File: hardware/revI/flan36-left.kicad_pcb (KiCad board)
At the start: 2 copper layers, 113.4 x 91.3 mm, 46 parts, among them J1 BATTERY_PIGTAIL, J2 nice!view, K01 KEYSW, K02 KEYSW, K03 KEYSW, K04 KEYSW, K05 KEYSW, K11 KEYSW, K12 KEYSW, K13 KEYSW, K14 KEYSW, K15 KEYSW, K21 KEYSW, K22 KEYSW, K23 KEYSW, K24 KEYSW, K25 KEYSW, K30 KEYSW, K31 KEYSW, K32 KEYSW, SW1 SW_SPDT_PCM12, SW2 SW_SPST_TL3342, U1 nice!nano v2

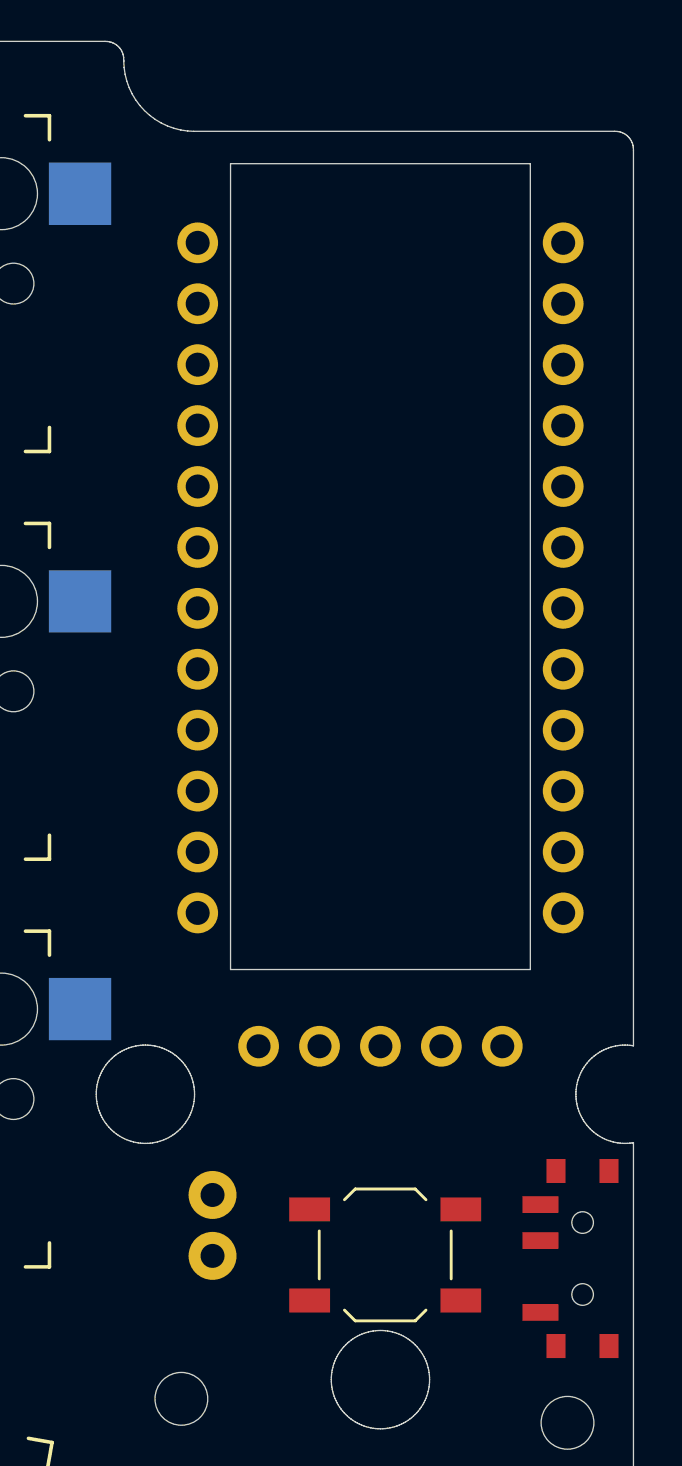
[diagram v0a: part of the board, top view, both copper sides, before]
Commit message: Lower electronics stack and add flush multicolor frame inlays
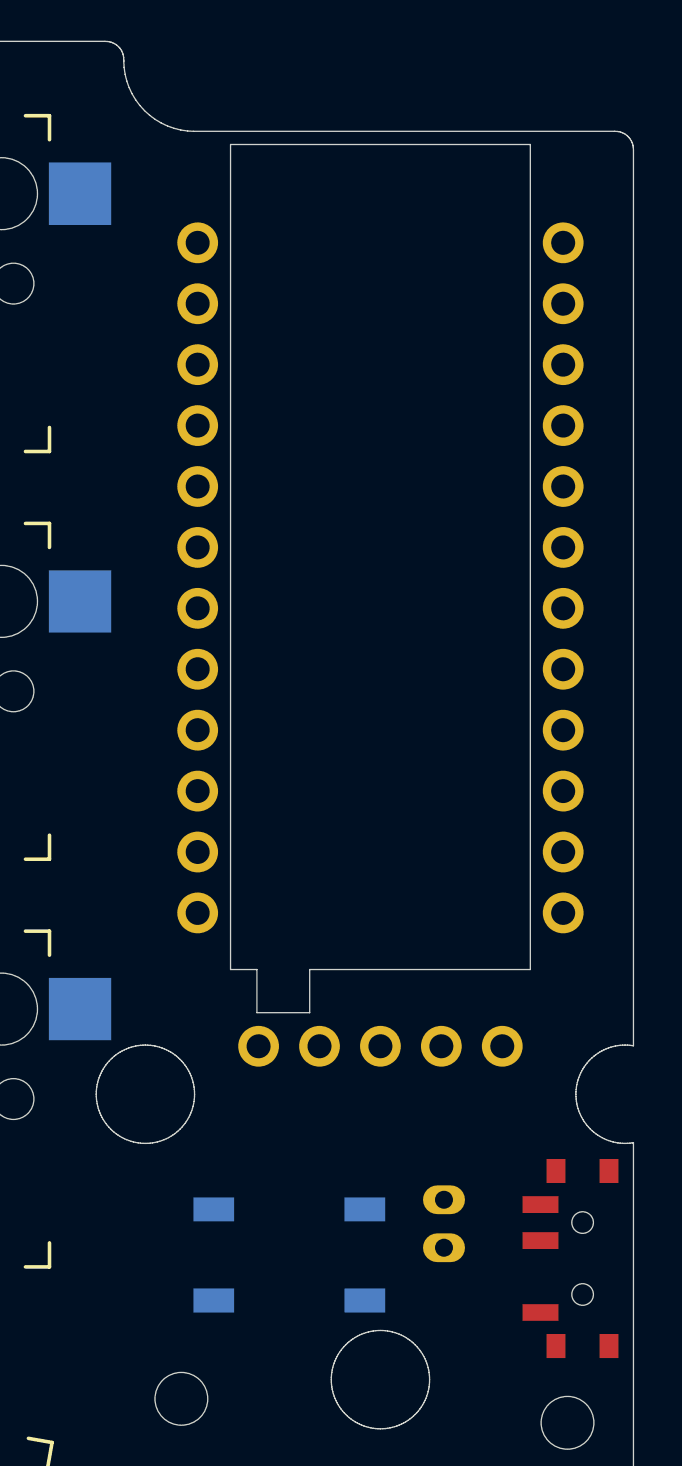
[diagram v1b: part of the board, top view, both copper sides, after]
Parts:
- J1: value BATTERY_PIGTAIL -> JST_PH_S2B-PH-K-S; footprint PiantorSlim:Battery_pigtail_2.54 -> PiantorSlim:JST_PH_S2B-PH-K_1x02_P2.00mm_Horizontal
- SW2: moved to B.Cu
- moved J1 9.65 mm to (125.5, 57.2), turned to 270 degrees
- moved SW2 4.00 mm to (119.0, 59.5)
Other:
- outline, holes or cut-outs redrawn

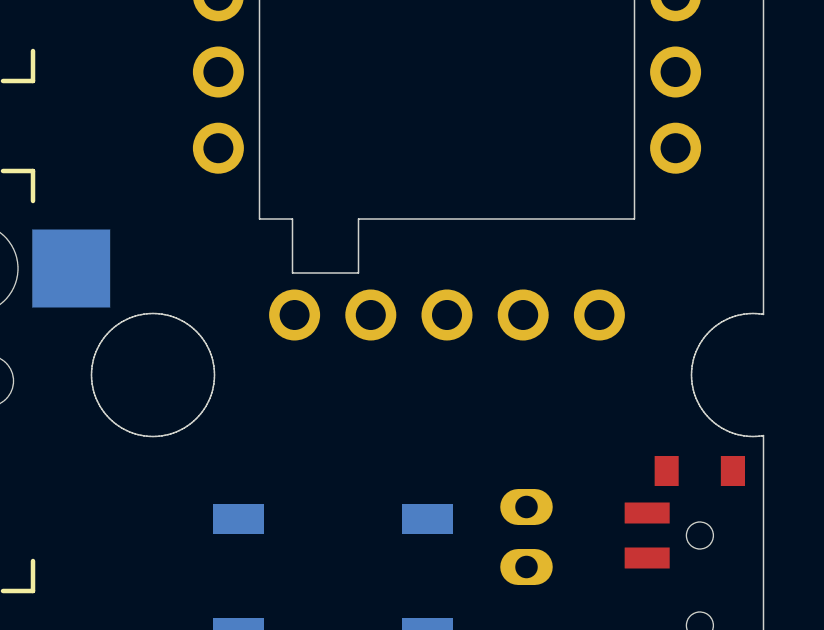
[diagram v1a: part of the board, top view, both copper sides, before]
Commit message: Implement five approved R4 frames with exact CAD and print geometry
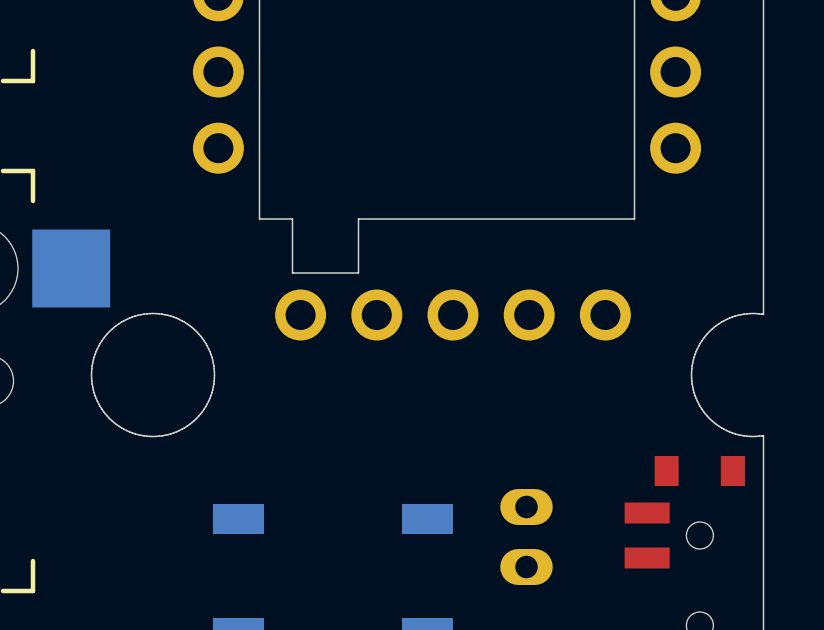
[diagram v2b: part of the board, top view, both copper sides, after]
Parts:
- moved J2 0.20 mm to (117.9, 50.8)
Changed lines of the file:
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@@
 	(footprint "PiantorSlim:nice_view_5pin"
 		(layer "F.Cu")
-		(at 117.72 50.8)
+		(at 117.920000 50.8)
 		(property "Reference" "J2"
 			(at 0 0 0)
